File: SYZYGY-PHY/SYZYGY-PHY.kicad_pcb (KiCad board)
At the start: 4 copper layers, 57.7 x 27 mm, 49 parts, among them J1 QTH-020-01-X-D-DP-A, J2 ARJM11C7-502-KB-EW2, J3 Conn_01x11, J4 Conn_01x02, U1 GPY111, U2 TXB0106RGY, U3 TXB0106RGY, Y1 Crystal_GND24

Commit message: syzygy phy docs
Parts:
- moved C1 27.7 mm to (105.3, 74.3)
- moved C12 27.7 mm to (87.3, 61.5)
- moved C13 27.7 mm to (88.7, 66.3)
- moved C14 27.7 mm to (87.8, 71.0)
- moved C16 27.7 mm to (87.8, 59.5)
- moved C18 27.7 mm to (90.1, 59.5)
- moved C2 27.7 mm to (101.4, 67.1)
- moved C25 27.7 mm to (105.3, 77.1)
- moved C26 27.7 mm to (90.3, 58.7)
- moved C7 27.7 mm to (92.0, 80.4)
- moved C8 27.7 mm to (92.1, 71.0)
- moved C9 27.7 mm to (98.4, 71.2)
- moved H1 27.7 mm to (67.1, 59.8)
- moved H2 27.7 mm to (117.1, 79.8)
- moved H3 27.7 mm to (117.1, 63.8)
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
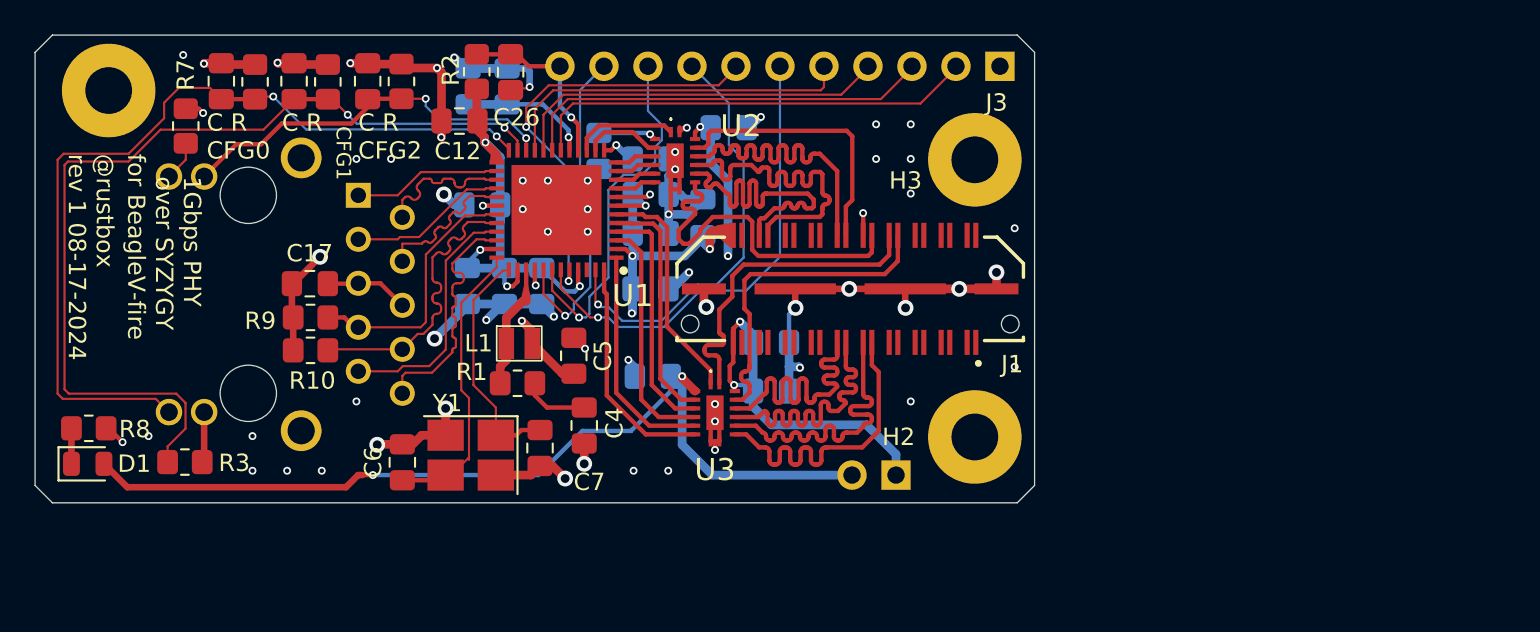
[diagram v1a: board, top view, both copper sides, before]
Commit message: updating gitignore and SYZYGY-PHY boards and footprints, and updating README with info on strapping pins and values
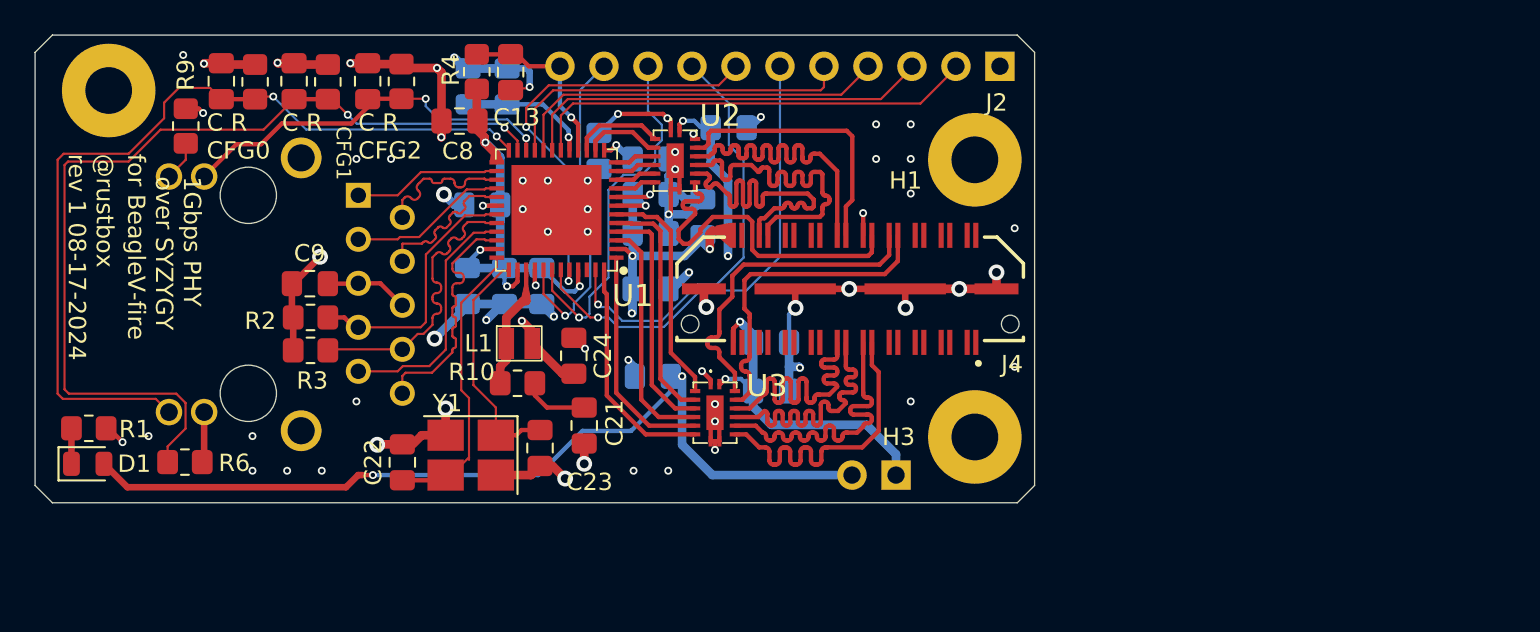
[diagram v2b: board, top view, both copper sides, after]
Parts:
- U2, U3: value TXB0106RGY -> TXV0106BQBR
- renumbered C8 to C1, C13 to C10, C14 to C11, C15 to C12, C26 to C13, C21 to C14, C20 to C15, C22 to C16, C3 to C17, C24 to C18, C23 to C19, C16 to C2, C25 to C20, C4 to C21, C6 to C22, C7 to C23, C5 to C24, C1 to C25, C2 to C26, C9 to C3, C18 to C4, C10 to C5, C19 to C6, C11 to C7, C12 to C8, C17 to C9, H3 to H1, H1 to H2, H2 to H3, J2 to J1, J3 to J2, J4 to J3, J1 to J4, R8 to R1, R1 to R10, R9 to R2, R10 to R3, R2 to R4, R4 to R5, R3 to R6, R5 to R7, R6 to R8, R7 to R9
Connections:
- U2 pad 1: /TX_CTL -> +3V3
- U2 pad 15: +1V8 -> /TX_CTL_L
- U2 pad 16: /TX_CTL_L -> +1V8
- U2 pad 2: +3V3 -> /TX_CTL
- U3 pad 1: /RX_CLK -> +3V3
- U3 pad 15: +1V8 -> /RX_CLK_L
- U3 pad 16: /RX_CLK_L -> +1V8
- U3 pad 2: +3V3 -> /RX_CLK
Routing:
- net +3V3: track 116.2 -> 120.0 mm, vias 12 -> 14
- net /TX_CTL_L: track 14.3 -> 13.3 mm
- net +1V8: track 34.8 -> 33.9 mm
- net /TX_CTL: track 6.03 -> 5.32 mm

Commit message: board updates, length tuning again
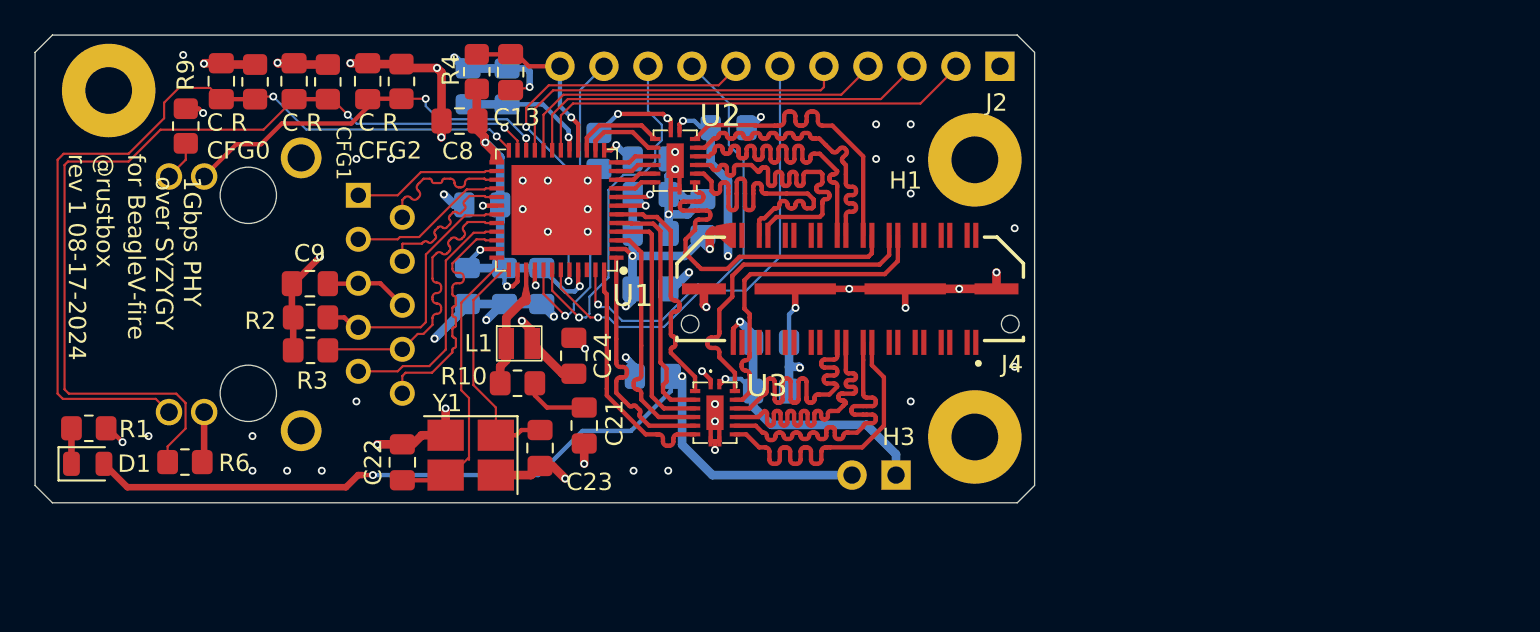
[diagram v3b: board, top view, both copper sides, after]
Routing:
- net /TX_CTL_L: track 13.3 -> 17.6 mm, vias 2 -> 0
- net /TXD0_L: track 15.8 -> 18.2 mm
- net /RXD3: track 13.1 -> 14.2 mm
- net /RX_CTL: track 13.3 -> 14.2 mm
- net /RX_CLK: track 13.4 -> 14.2 mm
- net /RXD0: track 13.8 -> 14.3 mm

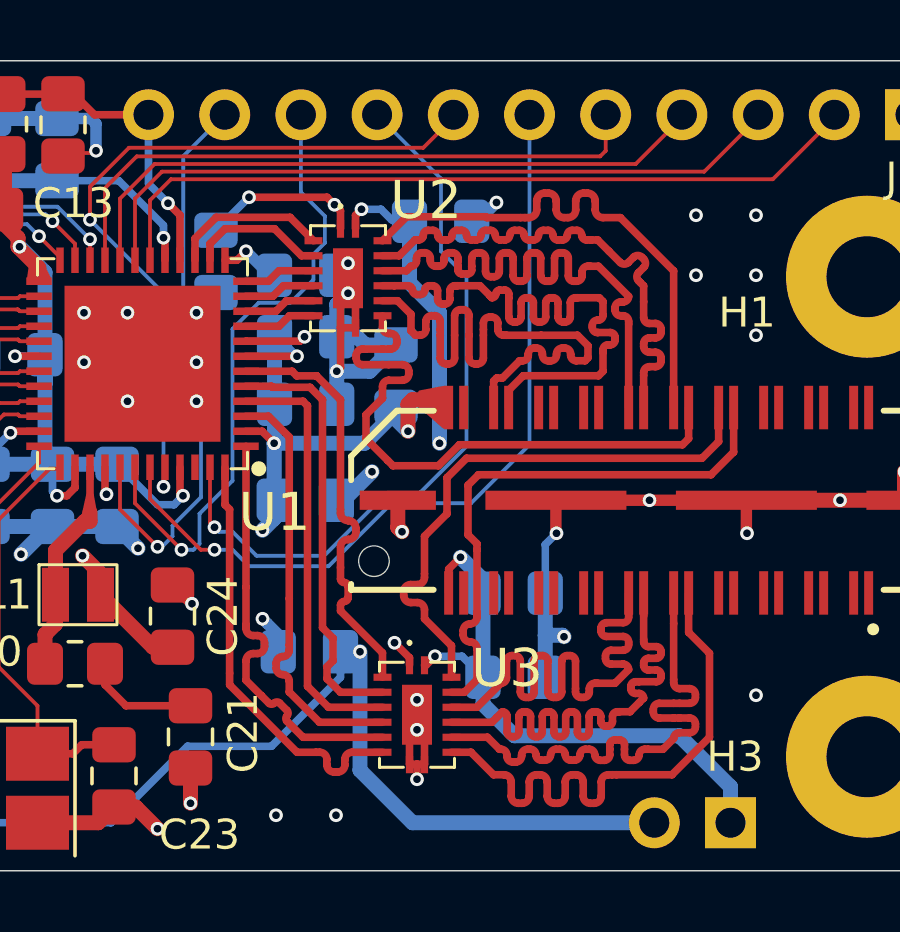
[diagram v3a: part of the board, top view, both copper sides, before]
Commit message: nfc: add some mouser numbers, quiet some warnings
Also, updated the RJ45 jack's schematic symbol to show both LEDs in the
left side.

NFC=No Functional Changes
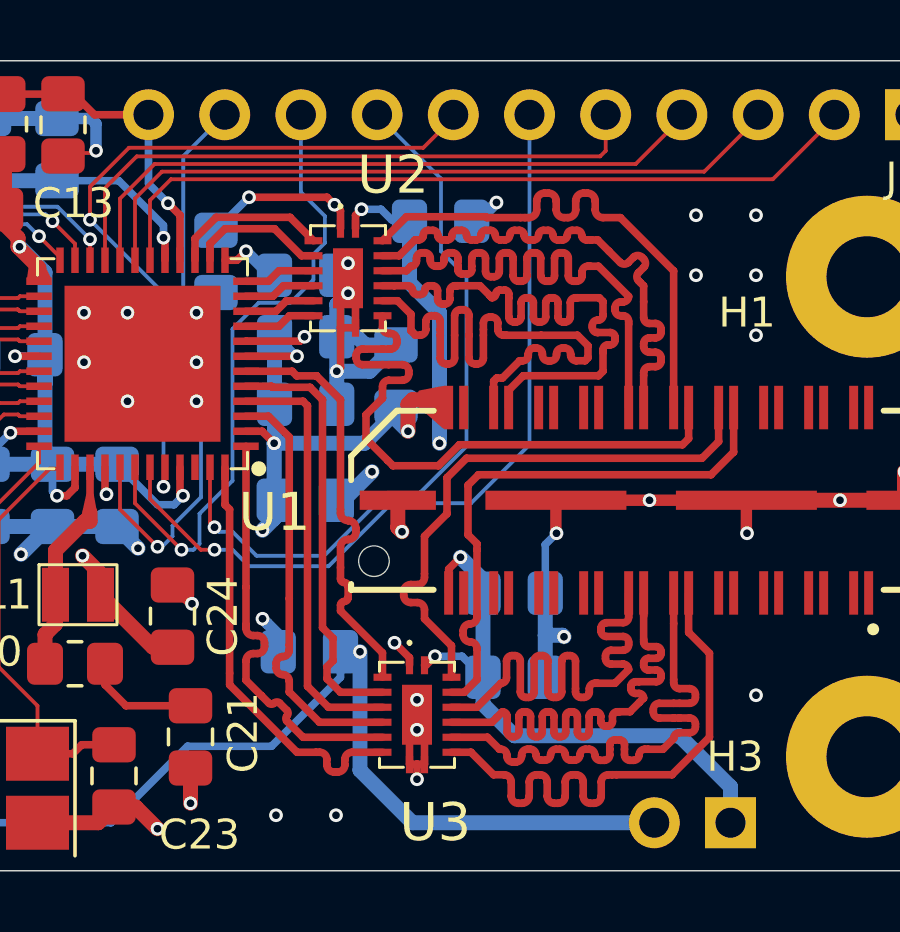
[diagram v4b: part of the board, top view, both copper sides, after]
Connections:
- net /LEFT_AN renamed /LEFT_GR_AN
